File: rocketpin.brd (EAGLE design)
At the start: 30.9 x 58.4 mm, 5 parts

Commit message: v2, ordered from seeed studio spring 2017
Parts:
- added U$1: (no value), LBR Logo:LOGO-0.50"
- R1: value (none) -> 47R
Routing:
- net N$1: track 0.00 -> 66.5 mm
- net GND: track 0.00 -> 34.0 mm
- net N$3: track 0.00 -> 29.3 mm
- net N$5: track 0.00 -> 25.7 mm
- net N$2: track 0.00 -> 9.72 mm

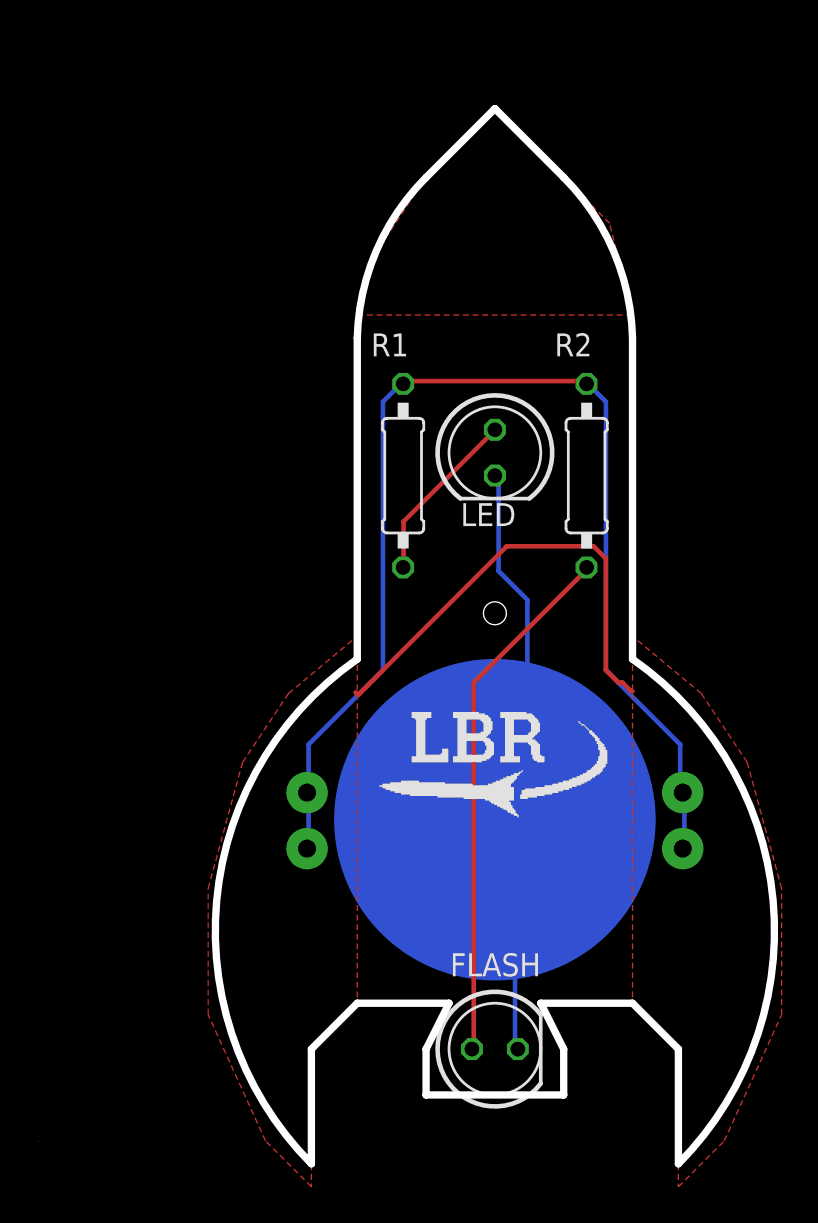
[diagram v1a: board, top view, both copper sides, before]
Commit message: changed size to add button
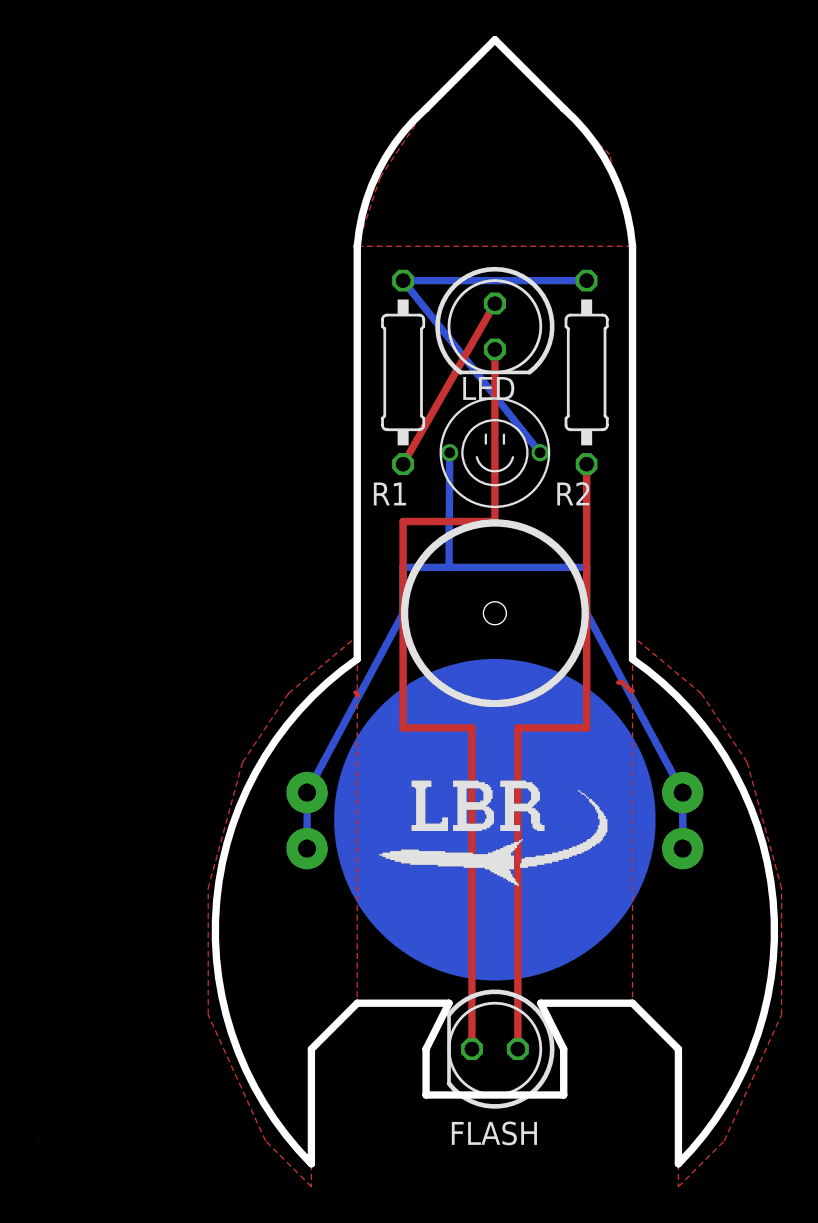
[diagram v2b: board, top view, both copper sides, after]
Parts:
- added U$3: EVQ-11D05B, switch:SPST-5MM
- moved LED 6.98 mm to (25.4, 45.1)
- moved R1 5.72 mm to (20.3, 42.5)
- moved R2 5.72 mm to (30.5, 42.5)
- moved U$1 3.81 mm to (19.1, 14.0)
- turned FLASH to 180 degrees
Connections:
- new net N$6: U$2.P$1, U$2.P$2, U$2.P$3, U$2.P$4, U$3.P$1
- net N$1: now also U$3.P$2; no longer U$2.P$1, U$2.P$2, U$2.P$3, U$2.P$4
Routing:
- net N$6: track 0.00 -> 50.3 mm
- net N$1: track 66.5 -> 22.3 mm
- net N$5: track 25.7 -> 1.18 mm
- net GND: track 34.0 -> 47.6 mm
- net N$3: track 29.3 -> 36.2 mm
- net N$2: track 9.72 -> 10.2 mm
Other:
- board size 30.9 x 58.4 mm -> 30.9 x 62.2 mm

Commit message: modify rocket pin
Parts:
- moved R1 0.64 mm to (20.3, 41.9)
- moved R2 0.64 mm to (30.5, 41.9)
- moved U$2 0.64 mm to (25.4, 17.1)
- moved LED 0.63 mm to (25.4, 44.5)
- moved U$3 0.63 mm to (25.4, 37.5)
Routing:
- net N$5: track 1.18 -> 24.3 mm
- net GND: track 47.6 -> 61.6 mm, vias 0 -> 1
- net N$3: track 36.2 -> 35.6 mm
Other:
- board size 30.9 x 62.2 mm -> 30.9 x 60.3 mm

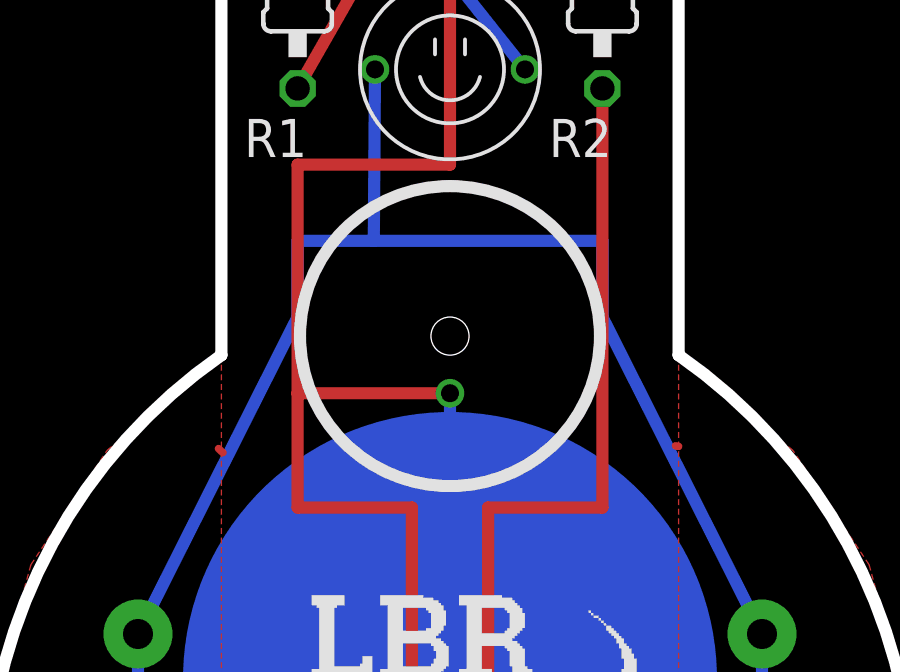
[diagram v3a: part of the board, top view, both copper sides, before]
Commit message: changed unicorn schematic so that all leds are in parallel with each other
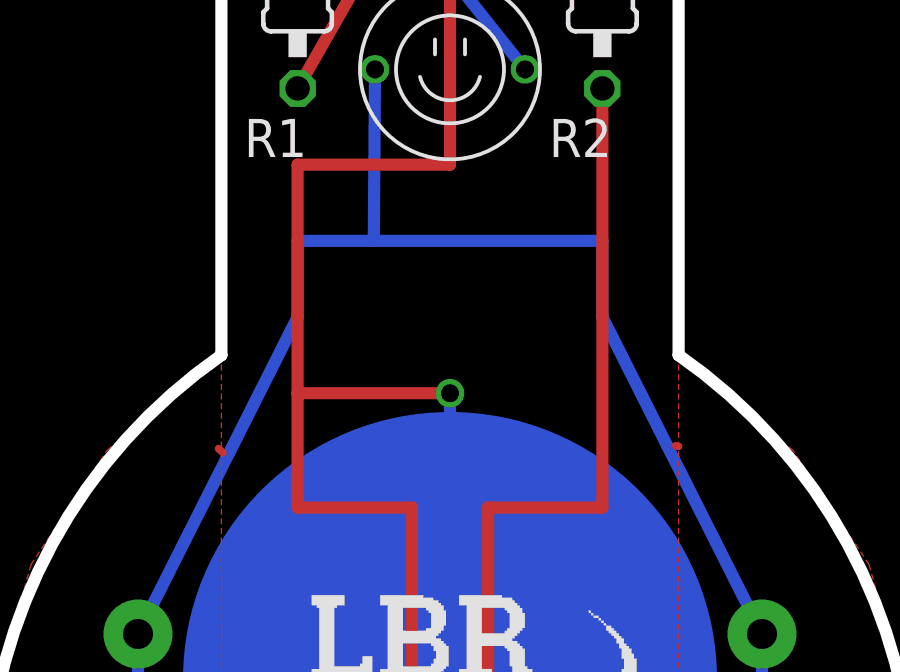
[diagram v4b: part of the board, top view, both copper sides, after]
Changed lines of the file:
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@@
 <rectangle x1="8.255" y1="-2.54" x2="18.415" y2="27.94" layer="29"/>
 <rectangle x1="32.385" y1="-2.54" x2="42.545" y2="27.94" layer="29"/>
-<hole x="25.4" y="28.575" drill="1.27"/>
-<circle x="25.4" y="28.575" radius="5" width="0.4064" layer="21"/>
+<circle x="25.4" y="28.575" radius="5" width="0.4064" layer="22"/>
 </plain>
 <attributes>
